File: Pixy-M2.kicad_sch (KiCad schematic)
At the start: 57 parts, among them J10 SM09B-SRSS-TB, J4 SM06B-SRSS-TB, J5 SM06B-SRSS-TB, J6 SM06B-SRSS-TB, J7 SM06B-SRSS-TB, J8 SM06B-SRSS-TB, J9 SM06B-SRSS-TB, Q1 AO4407A, SW3 JS102011SAQN, U1 ESP32-S3-DevKitC-1-N8R8, U3 AP63203WU, U4 DRV8231ADSG, U5 DRV8231ADSG

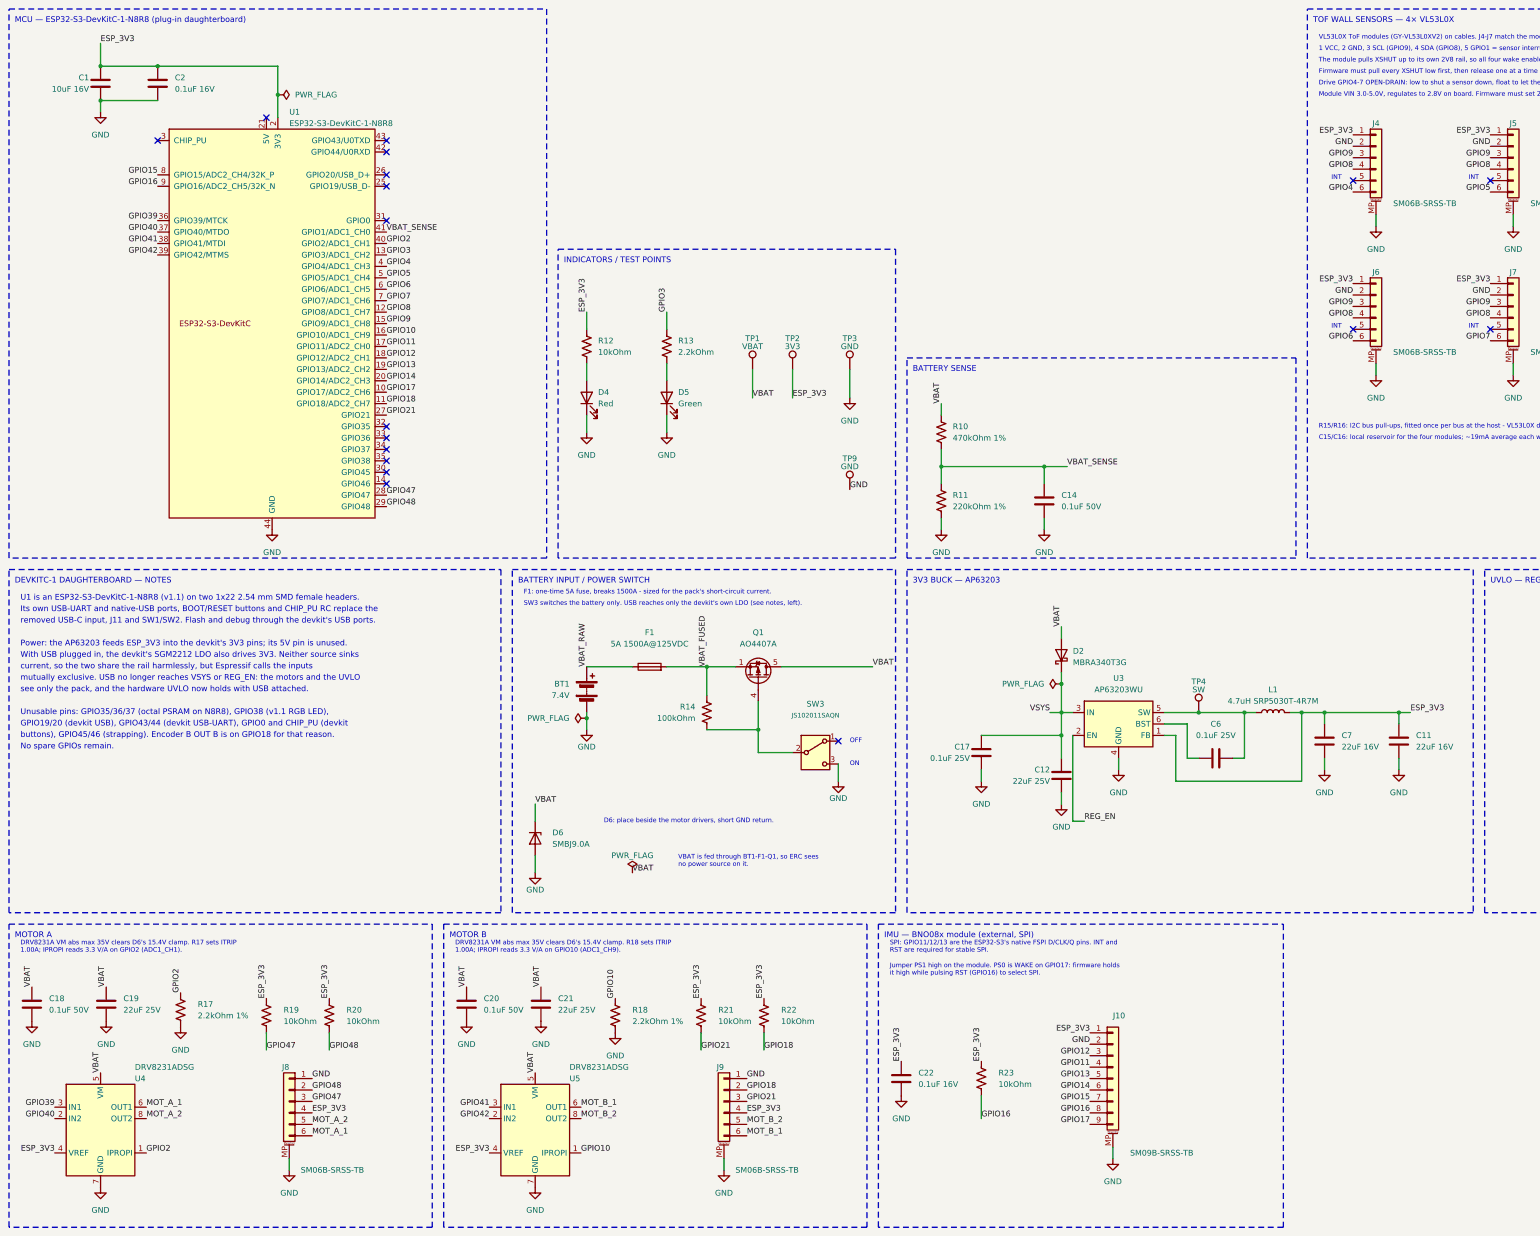
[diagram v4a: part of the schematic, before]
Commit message: power: independent motor cutoff, 1.242 V current reference, USB-priority isolation
Three supply problems on the devkit board:
- R7/R8 disable only the buck, so USB could keep the ESP32 alive and driving
  the motors from a flat pack.
- U4/U5 VREF came from the 3V3 rail, so the current limit followed the rail.
- The buck output was tied straight to the devkit's 3V3 pins, so USB and the
  buck fed one rail.

Schematic (tools/schematic/power_integrity.py; part data in
tools/power_integrity_data.py):
- U6 TLV3012B watches VBAT through R24/R25/R26 (100 k / 23.2 k / 825 k,
  0.1 %, 25 ppm/C) against its 1.242 V reference. U7 SN74LV4066A disconnects
  GPIO39-42 from the drivers below 6.35 V and reconnects them above 6.75 V,
  so the drivers' pulldowns coast both motors whatever USB or firmware do.
  The DC envelopes are 6.01-6.74 V (coast) and 6.39-7.08 V (enable).
- MOTOR_VREF from U6's REF feeds U4/U5 VREF. R17/R18 are now 1 k 1 %:
  ITRIP 0.828 A nominal, IPROPI 1.5 V/A. C25 (2.2 nF) at U6 and C28 (4.7 nF)
  at the driver split stay under the REF's 10 nF limit.
- BUCK_3V3 reaches ESP_3V3 through U8 LM66100 and Q2 AO3401A (opposing body
  diodes, Q3 following U8 ST). The devkit's 5V pin (U1.21) is sensed through
  R28/R29, giving USB priority. C30 (100 uF) carries ESP_3V3 through U8's
  turn-on at USB unplug.
- TP10 (MOTOR_OK), TP11 (MOTOR_VREF). Project symbol library Pixy-M2.kicad_sym.
- 72 nets, 79 parts, ERC 0. tools/power_integrity_check.py audits all 278
  pins, every part's fields and the DC corners.

Layout (new rework stage 21, tools/autoroute/power_integrity.py):
- The parts sit in clusters that keep the existing corridors free:
  - the USB switch in front of the devkit's USB end, fed straight from L1.2
    with no via;
  - U6/U7 and the divider at the rear, between the socket rows;
  - C28 and TP11 beside the motor corner;
  - TP2/TP3 moved between J5 and J7.
- Every re-routable net a cluster displaces is ripped whole and routed again.
  A first version patche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
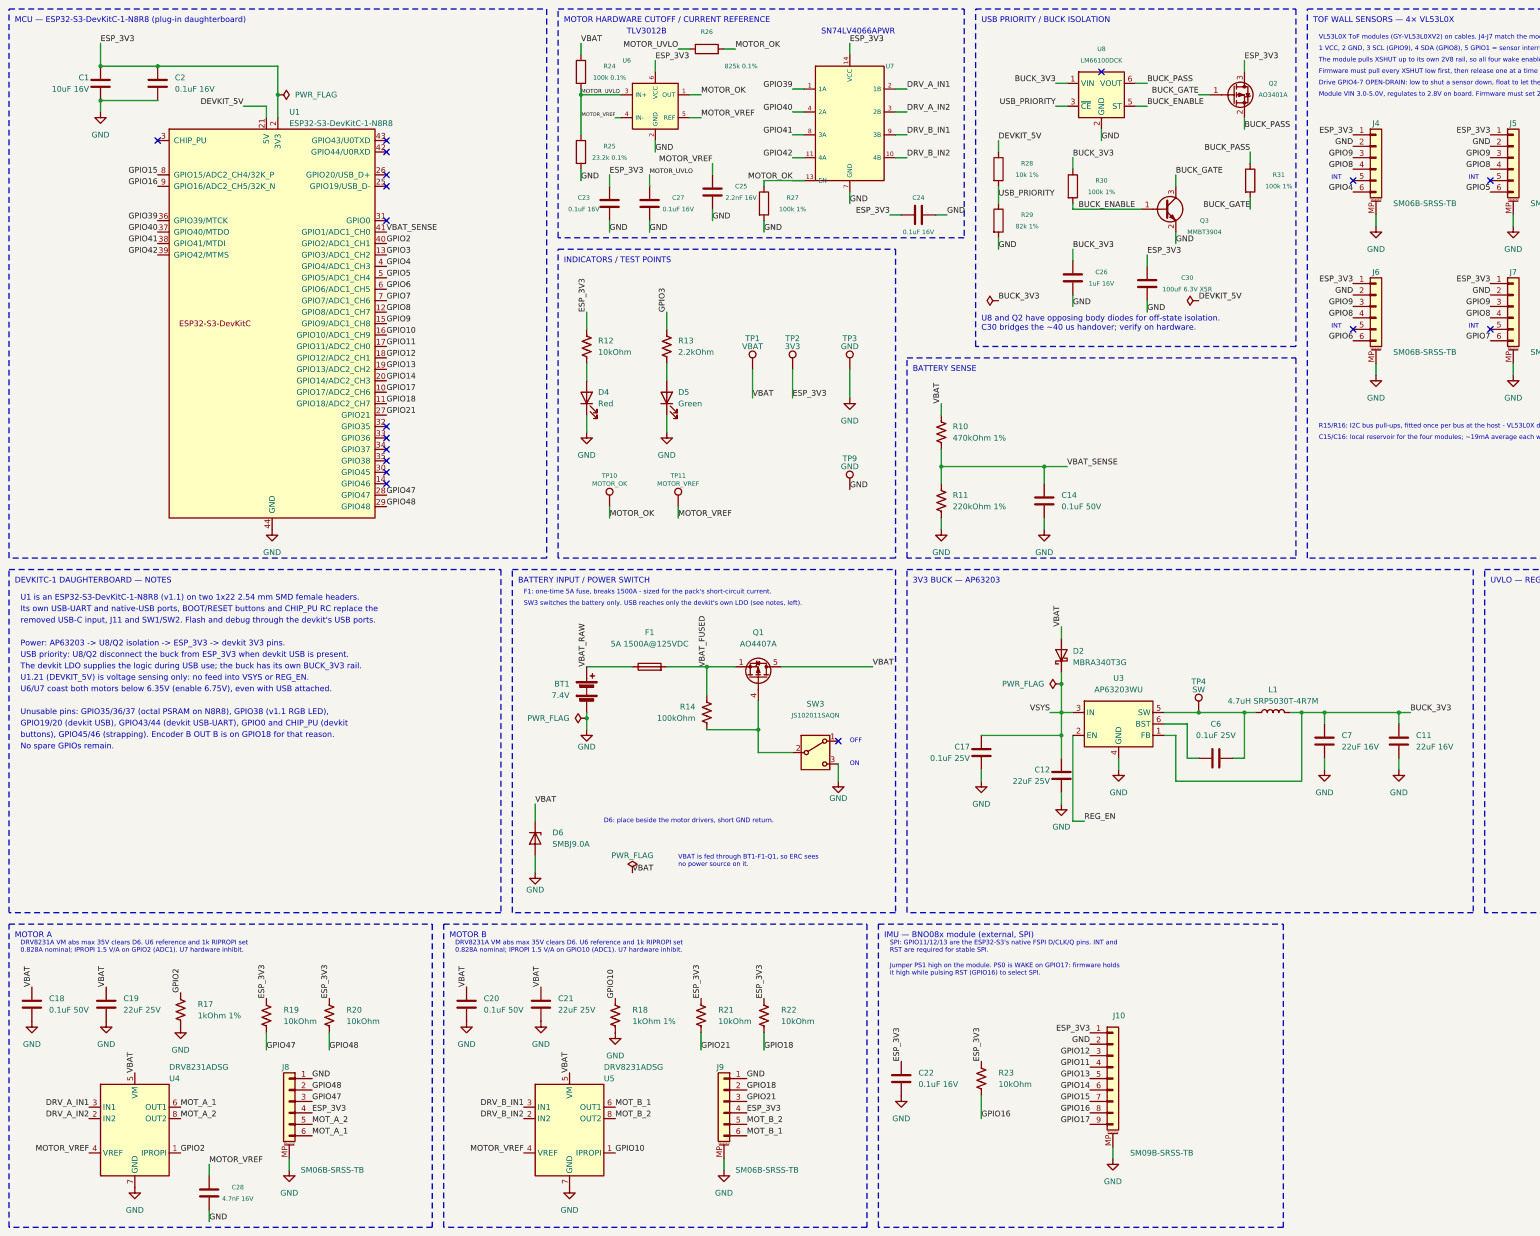
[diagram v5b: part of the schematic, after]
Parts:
- added C23, C24, C27: 0.1uF 16V, Capacitor_SMD:C_0603_1608Metric, symbol Device:C
- added C25: 2.2nF 16V, Capacitor_SMD:C_0603_1608Metric, symbol Device:C
- added C26: 1uF 16V, Capacitor_SMD:C_0603_1608Metric, symbol Device:C
- added C28: 4.7nF 16V, Capacitor_SMD:C_0603_1608Metric, symbol Device:C
- added C30: 100uF 6.3V X5R, Capacitor_SMD:C_1206_3216Metric, symbol Device:C
- added Q2: AO3401A, Package_TO_SOT_SMD:SOT-23, symbol Transistor_FET:AO3401A
- added Q3: MMBT3904, Package_TO_SOT_SMD:SOT-23, symbol Transistor_BJT:MMBT3904
- added R24: 100k 0.1%, Resistor_SMD:R_0805_2012Metric, symbol Device:R
- added R25: 23.2k 0.1%, Resistor_SMD:R_0805_2012Metric, symbol Device:R
- added R26: 825k 0.1%, Resistor_SMD:R_0805_2012Metric, symbol Device:R
- added R27, R30, R31: 100k 1%, Resistor_SMD:R_0805_2012Metric, symbol Device:R
- added R28: 10k 1%, Resistor_SMD:R_0805_2012Metric, symbol Device:R
- added R29: 82k 1%, Resistor_SMD:R_0805_2012Metric, symbol Device:R
- added TP10: MOTOR_OK, TestPoint:TestPoint_Pad_D1.5mm, symbol Connector:TestPoint
- added TP11: MOTOR_VREF, TestPoint:TestPoint_Pad_D1.5mm, symbol Connector:TestPoint
- added U6: TLV3012B, Package_TO_SOT_SMD:SOT-23-6, symbol Pixy-M2:TLV3012BDBV
- added U7: SN74LV4066APW, Package_SO:TSSOP-14_4.4x5mm_P0.65mm, symbol Pixy-M2:SN74LV4066APW
- added U8: LM66100DCK, Package_TO_SOT_SMD:SOT-363_SC-70-6, symbol Power_Management:LM66100DCK
- R17, R18: value 2.2kOhm 1% -> 1kOhm 1%; MPN (none) -> RC0805FR-071KL
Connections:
- net ESP_3V3: now also C23.1, C24.1, C30.1, Q2.3 (D), U6.6 (VCC), U7.14 (VCC); no longer C11.1, C7.1, L1.2, U3.1 (FB), U4.4 (VREF), U5.4 (VREF)
- net GND: now also C23.2, C24.2, C25.2, C26.2, C27.2, C28.2, C30.2, Q3.2 (E), R25.2, R27.2, R29.2, U6.2 (GND), U7.7 (GND), U8.2 (GND)
- net GPIO39: now also U7.1 (1A); no longer U4.3 (IN1)
- net GPIO40: now also U7.4 (2A); no longer U4.2 (IN2)
- net GPIO41: now also U7.8 (3A); no longer U5.3 (IN1)
- net GPIO42: now also U7.11 (4A); no longer U5.2 (IN2)
- net VBAT: now also R24.1
- net DEVKIT_5V: now reaches U1.21 (5V)
- net DEVKIT_5V: now also R28.1
- new net BUCK_3V3: C11.1, C26.1, C7.1, L1.2, R30.1, U3.1 (FB), U8.1 (VIN)
- new net BUCK_ENABLE: Q3.1 (B), R30.2, U8.5 (ST)
- new net BUCK_GATE: Q2.1 (G), Q3.3 (C), R31.2
- new net BUCK_PASS: Q2.2 (S), R31.1, U8.6 (VOUT)
- new net DRV_A_IN1: U4.3 (IN1), U7.2 (1B)
- new net DRV_A_IN2: U4.2 (IN2), U7.3 (2B)
- new net DRV_B_IN1: U5.3 (IN1), U7.9 (3B)
- new net DRV_B_IN2: U5.2 (IN2), U7.10 (4B)
- new net MOTOR_OK: R26.2, R27.1, TP10.1, U6.1 (OUT), U7.12, U7.13 (EN), U7.5, U7.6
- new net MOTOR_UVLO: C27.1, R24.2, R25.1, R26.1, U6.3 (IN+)
- new net MOTOR_VREF: C25.1, C28.1, TP11.1, U4.4 (VREF), U5.4 (VREF), U6.4 (IN-), U6.5 (REF)
- new net USB_PRIORITY: R28.2, R29.1, U8.3 (~{CE})
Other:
- note added: "DRV8231A VM abs max 35V clears D6. U6 reference and 1k RIPROPI set 0.828A nominal; IPROPI 1.5 V/A on GPIO10 (ADC1). U7 hardware inhibit."
- note added: "DRV8231A VM abs max 35V clears D6. U6 reference and 1k RIPROPI set 0.828A nominal; IPROPI 1.5 V/A on GPIO2 (ADC1). U7 hardware inhibit."
- note added: "MOTOR HARDWARE CUTOFF / CURRENT REFERENCE"
- note added: "Power: AP63203 -> U8/Q2 isolation -> ESP_3V3 -> devkit 3V3 pins."
- note added: "SN74LV4066APWR"
- note added: "TLV3012B"
- note added: "The devkit LDO supplies the logic during USB use; the buck has its own BUCK_3V3 rail."
- note added: "U1.21 (DEVKIT_5V) is voltage sensing only: no feed into VSYS or REG_EN."
- note added: "U6/U7 coast both motors below 6.35V (enable 6.75V), even with USB attached."
- note added: "U8 and Q2 have opposing body diodes for off-state isolation. C30 bridges the ~40 us handover; verify on hardware."
- note added: "USB PRIORITY / BUCK ISOLATION"
- note added: "USB priority: U8/Q2 disconnect the buck from ESP_3V3 when devkit USB is present."
- note removed: "DRV8231A VM abs max 35V clears D6's 15.4V clamp. R17 sets ITRIP 1.00A; IPROPI reads 3.3 V/A on GPIO2 (ADC1_CH1)."
- note removed: "DRV8231A VM abs max 35V clears D6's 15.4V clamp. R18 sets ITRIP 1.00A; IPROPI reads 3.3 V/A on GPIO10 (ADC1_CH9)."
- note removed: "Power: the AP63203 feeds ESP_3V3 into the devkit's 3V3 pins; its 5V pin is unused."
- note removed: "With USB plugged in, the devkit's SGM2212 LDO also drives 3V3. Neither source sinks"
- note removed: "current, so the two share the rail harmlessly, but Espressif calls the inputs"
- note removed: "mutually exclusive. USB no longer reaches VSYS or REG_EN: the motors and the UVLO"
- note removed: "see only the pack, and the hardware UVLO now holds with USB attached."
- moved on the sheet: U4, U5
